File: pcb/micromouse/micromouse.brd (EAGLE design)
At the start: 80 x 115 mm, 66 parts, among them IC1 LM2575-5.0WU-(TR), IC2 LM2575-3.3WU-(TR), IC3 DSPIC33FJ64MC804-PT, IC4 L293D, Y1 7.3728MHz

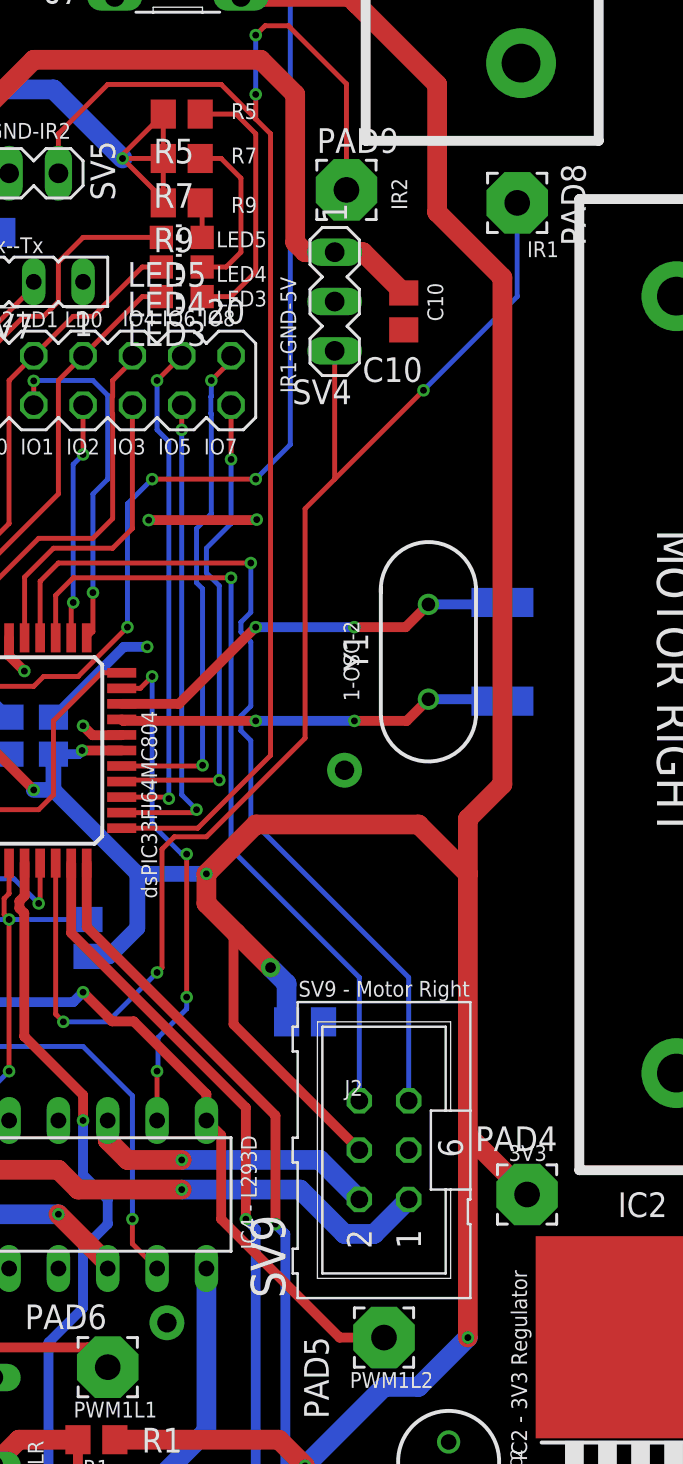
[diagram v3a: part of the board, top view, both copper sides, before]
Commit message: Intermediate state of moving of oscillator
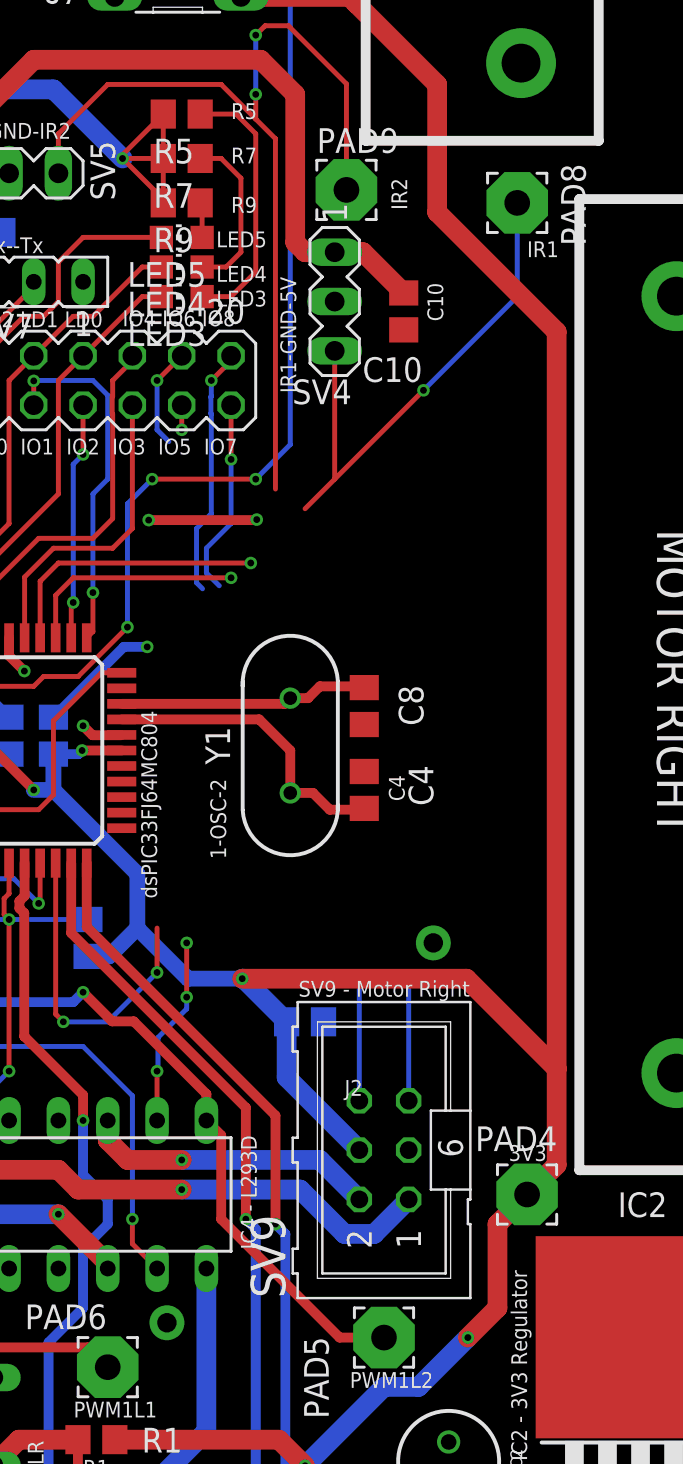
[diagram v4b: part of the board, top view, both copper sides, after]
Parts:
- moved C8 8.89 mm to (58.9, 56.9), flipped to the top, turned to 90 degrees
- moved Y1 8.59 mm to (55.1, 54.9)
- moved C4 8.45 mm to (58.9, 52.6), flipped to the top, turned to 270 degrees
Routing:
- net IR1: track 69.1 -> 43.4 mm
- net ENC2_B: track 46.0 -> 20.5 mm
- net IO5: track 25.1 -> 1.27 mm, vias 2 -> 1
- net ENC2_A: track 41.3 -> 17.9 mm
- net IR2: track 72.2 -> 49.3 mm
- net IO6: track 26.0 -> 5.19 mm, vias 2 -> 1
- net M2+_EN: track 26.2 -> 9.78 mm, vias 4 -> 3
- net IO7: track 25.2 -> 10.2 mm, vias 2 -> 1
- net IO8: track 26.1 -> 12.9 mm, vias 2 -> 1
- net +3V3: track 469.2 -> 460.8 mm, vias 12 -> 11
- net OSC2: track 20.8 -> 12.9 mm, vias 2 -> 0
- net OSC1: track 19.2 -> 15.7 mm, vias 2 -> 0

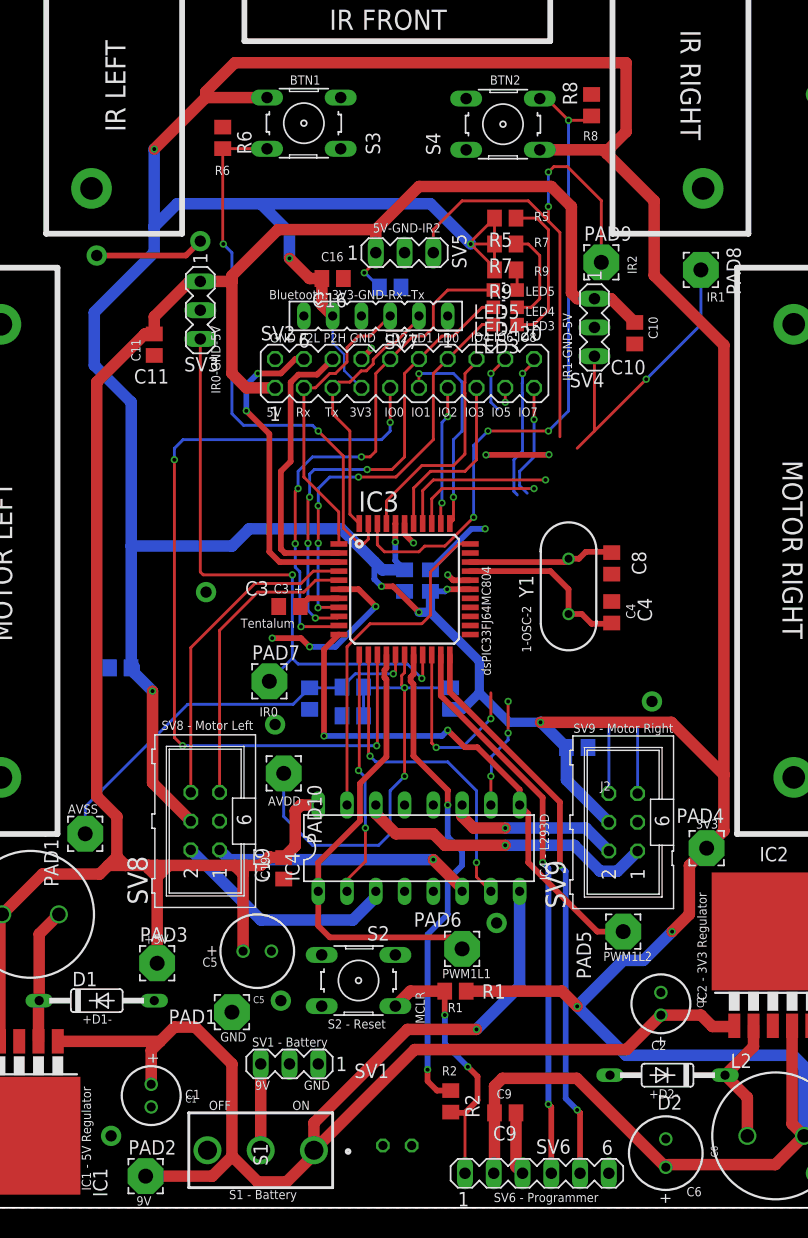
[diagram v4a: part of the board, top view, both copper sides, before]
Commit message: Finished wiring of oscialltor, few minor improvements and added missing silk labels
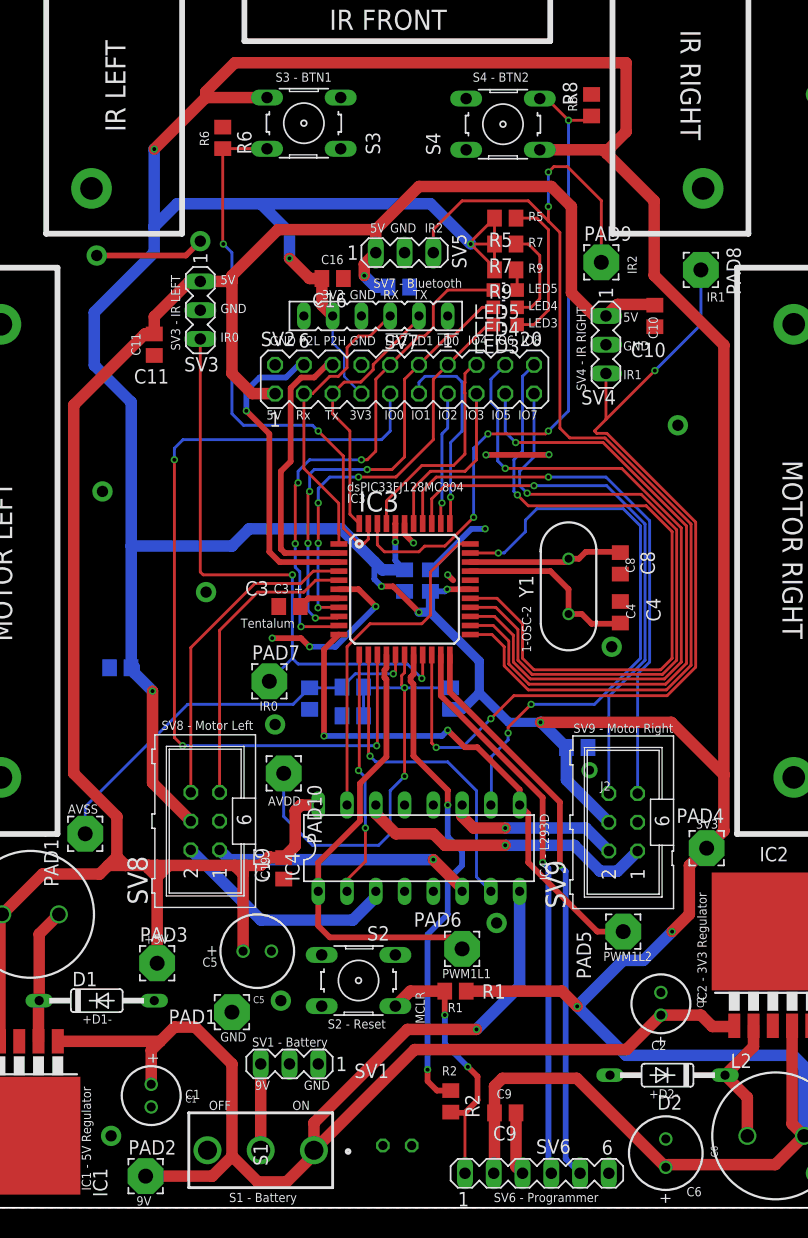
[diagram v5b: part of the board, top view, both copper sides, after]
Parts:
- moved C10 2.34 mm to (62.7, 78.7)
- moved SV4 1.83 mm to (58.4, 76.2)
- moved C12 0.76 mm to (40.1, 81.3)
- moved C4 0.76 mm to (59.7, 52.6)
- moved C8 0.76 mm to (59.7, 56.9)
- moved SV2 0.51 mm to (40.6, 73.2)
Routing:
- net IO6: track 5.19 -> 62.7 mm
- net IO5: track 1.27 -> 58.1 mm
- net IR2: track 49.3 -> 99.5 mm
- net IO8: track 12.9 -> 61.2 mm
- net IO7: track 10.2 -> 58.4 mm
- net M2+_EN: track 9.78 -> 51.3 mm
- net IR1: track 43.4 -> 81.4 mm
- net ENC2_A: track 17.9 -> 48.0 mm
- net ENC2_B: track 20.5 -> 49.6 mm
- net +5V: track 193.9 -> 198.7 mm
- net GND: track 47.5 -> 44.7 mm, vias 30 -> 32
- net OSC2: track 12.9 -> 13.7 mm
- net OSC1: track 15.7 -> 16.5 mm
- net PWM2L1: track 28.1 -> 27.6 mm, vias 2 -> 1
- net PWM2H1: track 24.9 -> 24.4 mm
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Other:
- board text added: "5V"
- board text added: "IC3"
- board text added: "R18"
- board text added: "RX"
- board text added: "S3 - BTN1"
- board text added: "S4 - BTN2"
- board text added: "SV3 - IR LEFT"
- board text added: "SV4 - IR RIGHT"
- board text added: "SV7 - Bluetooth"
- board text added: "TX"
- board text added: "dsPIC33FJ128MC804"
- board text removed: "5V-GND-IR2"
- board text removed: "BTN1"
- board text removed: "BTN2"
- board text removed: "Bluetooth: 3V3-GND-Rx--Tx"
- board text removed: "C18"
- board text removed: "IR0-GND-5V"
- board text removed: "IR1-GND-5V"
- board text removed: "dsPIC33FJ64MC804"

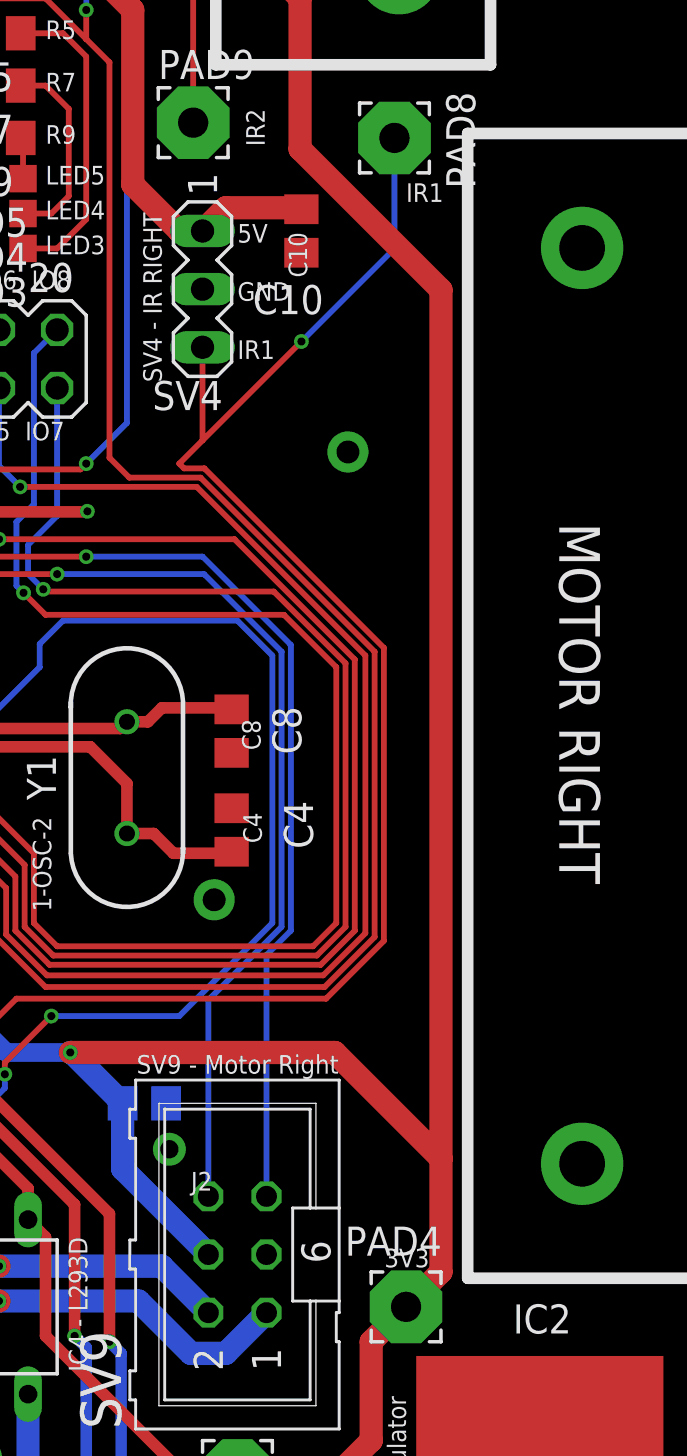
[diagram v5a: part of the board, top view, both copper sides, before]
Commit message: Add group name, move via next to oscillator and replace LEDs with low current LEDs.
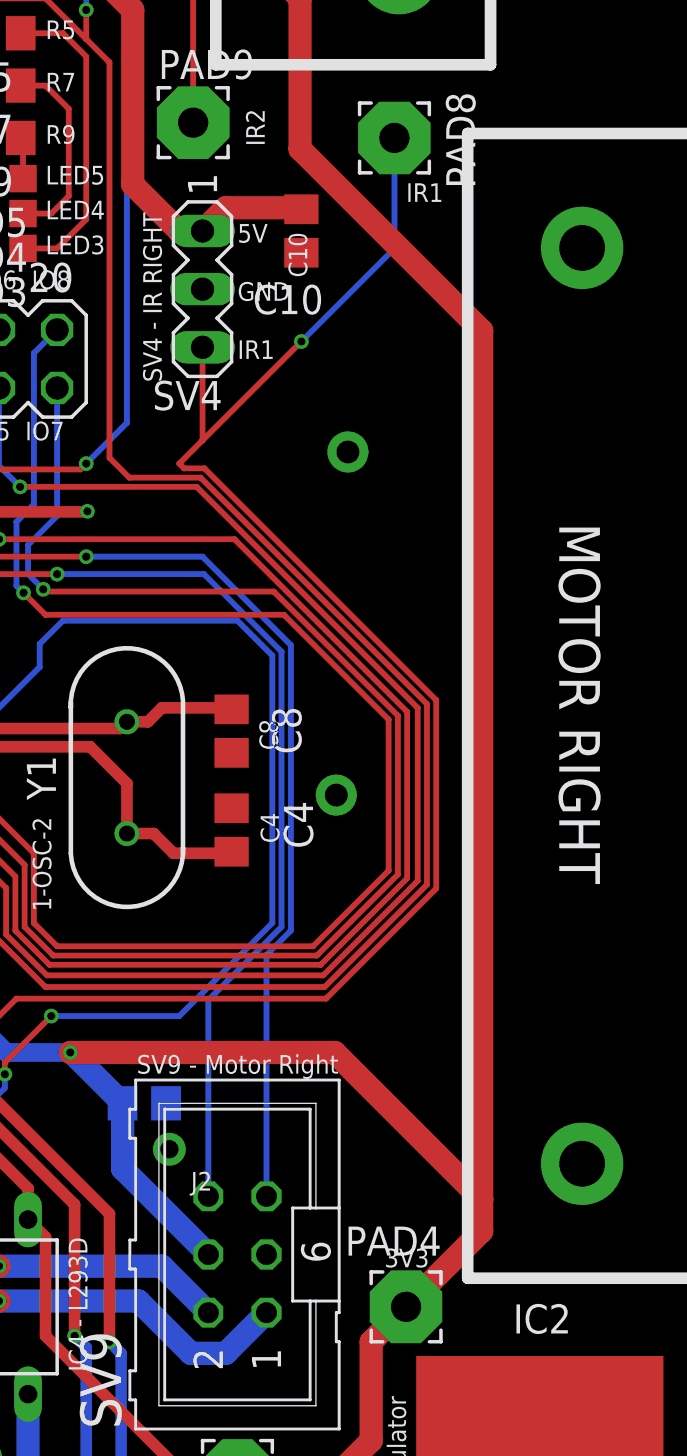
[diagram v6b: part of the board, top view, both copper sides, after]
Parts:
- R5, R7, R9: value 120R -> 680R
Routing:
- net +3V3: track 461.3 -> 465.3 mm
- net IO8: track 61.2 -> 63.1 mm
- net IR1: track 81.4 -> 83.3 mm
- net IO7: track 58.4 -> 60.3 mm
- net IO6: track 62.7 -> 64.6 mm
- net IO5: track 58.1 -> 60.0 mm
- net IR2: track 99.5 -> 101.4 mm
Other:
- board text added: "Micromouse WS22/23 Ludwig Stumpp Franz Kaschner Marwan Shalaby Hatem Elsayed"

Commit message: vias+beef gnds
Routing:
- net GND: track 44.7 -> 112.8 mm
- net +3V3: track 465.3 -> 501.3 mm, vias 11 -> 10
- net BTN_2: track 58.9 -> 56.9 mm
- net IR2: track 101.4 -> 102.5 mm
- net IO5: track 60.0 -> 61.0 mm
- net IO3: track 15.6 -> 14.7 mm
- net IO8: track 63.1 -> 62.3 mm
- net ENC2_A: track 48.0 -> 48.7 mm
- net IO4: track 19.1 -> 18.5 mm
- net PGED1: vias 1 -> 2
- net PGEC1: vias 1 -> 2
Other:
- board text added: "-D2+"
- board text added: "C18"
- board text removed: "+D2-"
- board text removed: "R18"

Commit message: pcb remarks solve 3V3 branch other side no vias for 9v to H bridge beef gnd pins delete t/b Names make AVDD+AVSS closer better path under uc vias near oscilator, controller and controller voltage regulator output voltage connected to capacitor not inductor rotate diodes to have it's ground near to regulator ground rectivy angles and errors+design rules
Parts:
- moved D2 8.74 mm to (72.4, 13.6), turned to 0 degrees
- moved D1 5.85 mm to (7.62, 18.5), turned to 180 degrees
- moved R1 4.98 mm to (48.8, 15.7)
- moved PAD3 3.02 mm to (18.9, 24.6)
- moved R3 2.41 mm to (42.4, 44.2)
- moved C14 2.15 mm to (38.9, 56.6), turned to 180 degrees
- moved R4 1.77 mm to (34.0, 44.7)
- moved C7 1.33 mm to (37.4, 43.3)
- moved C13 1.32 mm to (37.4, 45.7)
- moved PAD4 1.30 mm to (67.3, 33.0)
- moved IC2 1.07 mm to (73.2, 22.9)
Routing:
- net GND: track 112.8 -> 150.7 mm, vias 32 -> 49
- net +5V: track 198.7 -> 207.4 mm
- net N_MCLR: track 24.0 -> 30.6 mm
- net N$1: track 47.6 -> 43.3 mm
- net N$8: track 11.6 -> 15.3 mm
- net N$7: track 12.0 -> 15.6 mm
- net AVDD: track 41.5 -> 38.2 mm
- net +9V: track 123.9 -> 126.5 mm, vias 1 -> 0
- net +3V3: track 501.3 -> 499.0 mm
- net M2+_EN: track 51.1 -> 53.2 mm
